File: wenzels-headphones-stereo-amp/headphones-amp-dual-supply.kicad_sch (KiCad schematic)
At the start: 70 parts, among them J1 9V-15V, J2 9V-15V, J3 Input, J4 Headphones out, Q1 BD139, Q2 BD140, Q3 BD139, Q4 BD140, SW1 POWER ON, U1 NE5532

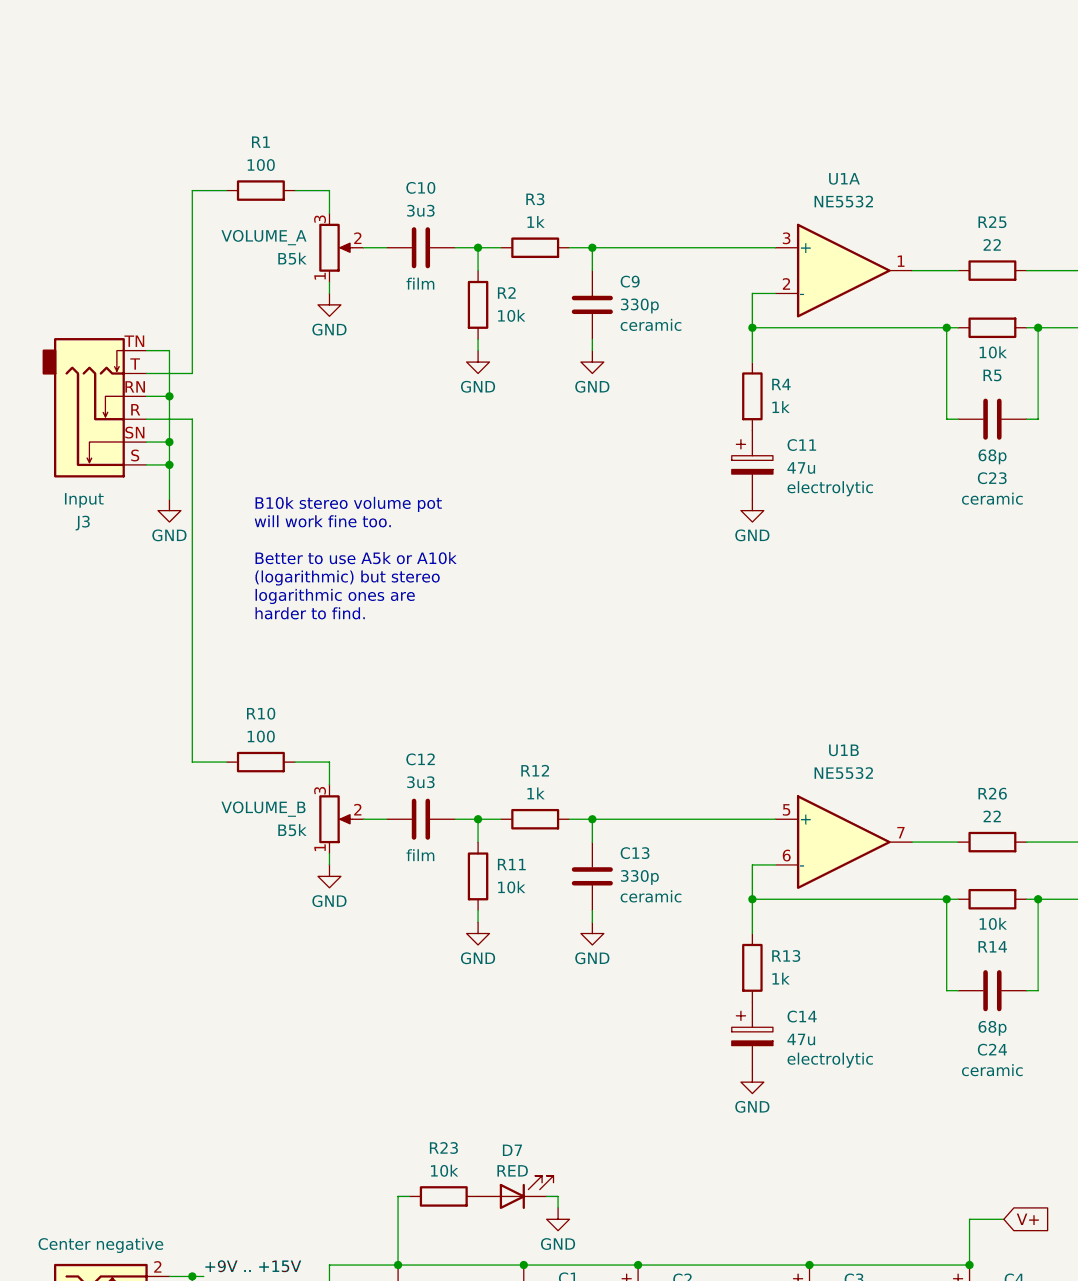
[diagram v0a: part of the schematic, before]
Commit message: wenzels-headphones-stereo-amp: Add GAIN knob
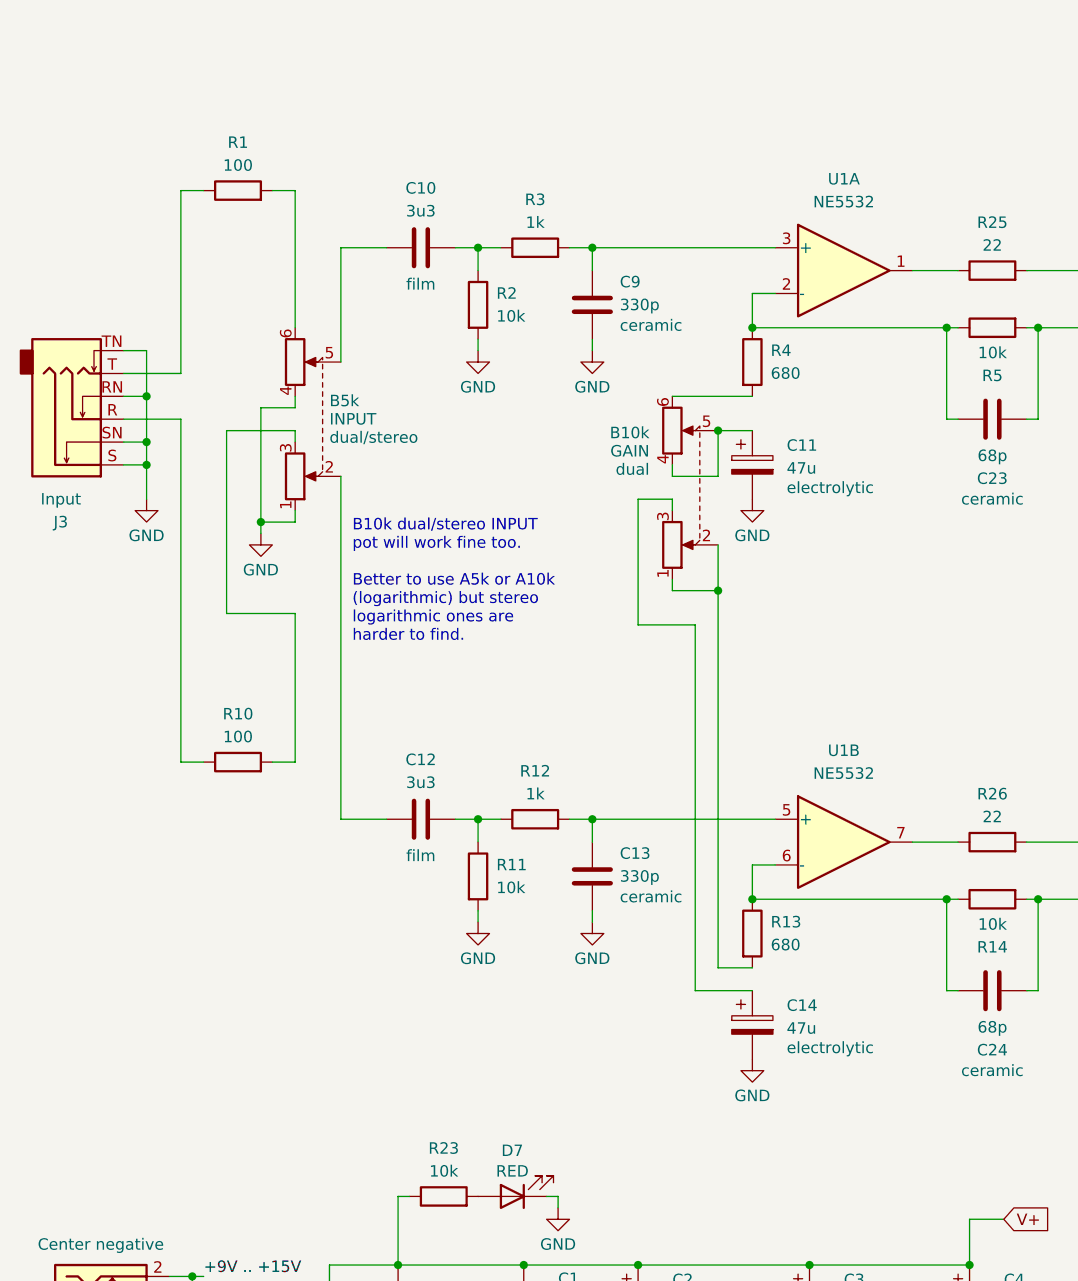
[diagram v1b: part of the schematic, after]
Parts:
- removed VOLUME_A, VOLUME_B: B5k, symbol Device:R_Potentiometer
- added GAIN: B10k, symbol Device:R_Potentiometer_Dual
- added INPUT: B5k, symbol Device:R_Potentiometer_Dual
- R13, R4: value 1k -> 680
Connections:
- net GND: now also INPUT.1, INPUT.4
- net at R4.2: now also GAIN.6; no longer C11.1
- net at C12.1: now also INPUT.2
- net at R1.2: now also INPUT.6
- net at R10.2: now also INPUT.3
- net at C10.1: now also INPUT.5
- net at R13.2: now also GAIN.1, GAIN.2; no longer C14.1
- new net: C11.1, GAIN.4, GAIN.5
- new net: C14.1, GAIN.3
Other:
- note added: "B10k dual/stereo INPUT pot will work fine too. Better to use A5k or A10k (logarithmic) but stereo logarithmic ones are harder to find."
- note removed: "B10k stereo volume pot will work fine too. Better to use A5k or A10k (logarithmic) but stereo logarithmic ones are harder to find."
- moved on the sheet: C14, J3, R1, R10, R13, R4
